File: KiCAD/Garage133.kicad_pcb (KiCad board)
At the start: 4 copper layers, 82.5 x 39.4 mm, 44 parts, among them J1 Edge2x6_Connector, J2 USB_B_Micro, K1 SANYOU_SRD_Form_C, K2 SANYOU_SRD_Form_C, Q2 UMH3N, Q3 MMBT3906, Q4 MMBT3906, U1 ESP32-WROOM-32, U2 AMS1117-3.3, U3 SHTC3

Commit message: Updated KiCAD design
Fixes with help from Gemini.

- 2 sonars per side
- Divide-down echo signal to be 3V input-safe
- Fix pin assignments to non-straping pins for relay control, to avoid opening the garage
   door on power on(!)
- 1mm traces for relay nets, to be safer in case someone wires more power through these
   connections.
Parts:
- removed the REF** at (70.4, 50.8)
- removed the REF** at (141.0, 50.8)
- removed the REF** at (141.0, 85.1)
- removed the REF** at (80.3, 52.1)
- added J_SNR3: Conn_01x04_Pin, Connector_JST:JST_XH_B4B-XH-A_1x04_P2.50mm_Vertical, F.Cu at (120.8, 52.1)
- added J_SNR4: Conn_01x04_Pin, Connector_JST:JST_XH_B4B-XH-A_1x04_P2.50mm_Vertical, F.Cu at (120.8, 61.0)
- added R2l1: 2.2k, Resistor_SMD:R_0603_1608Metric, F.Cu at (81.9, 55.9)
- added R2l2: 2.2k, Resistor_SMD:R_0603_1608Metric, F.Cu at (80.0, 55.9)
- added R2l3: 2.2k, Resistor_SMD:R_0603_1608Metric, F.Cu at (125.2, 57.1)
- added R2l4: 2.2k, Resistor_SMD:R_0603_1608Metric, F.Cu at (126.4, 66.7)
- added R3l1: 3.3k, Resistor_SMD:R_0603_1608Metric, F.Cu at (83.8, 55.9)
- added R3l2: 3.3k, Resistor_SMD:R_0603_1608Metric, F.Cu at (78.1, 55.9)
- added R3l3: 3.3k, Resistor_SMD:R_0603_1608Metric, F.Cu at (122.2, 57.1)
- added R3l4: 3.3k, Resistor_SMD:R_0603_1608Metric, F.Cu at (128.3, 66.7)
- added REF**: MountingHole_2.5mm, MountingHole:MountingHole_2.5mm, F.Cu at (156.2, 85.1)
- added REF**: MountingHole_2.5mm, MountingHole:MountingHole_2.5mm, F.Cu at (80.0, 51.4)
- added REF**: MountingHole_2.5mm, MountingHole:MountingHole_2.5mm, F.Cu at (156.2, 50.8)
- added REF**: MountingHole_2.5mm, MountingHole:MountingHole_2.5mm, F.Cu at (70.5, 50.8)
- added RTRL3: 1k, Resistor_SMD:R_0603_1608Metric, F.Cu at (69.2, 55.2)
- added RTRL4: 1k, Resistor_SMD:R_0603_1608Metric, F.Cu at (123.2, 66.7)
- J1: footprint Library:EdgeConnector_2x3 -> chl33_library:EdgeConnector_2x3
- moved K2 15.4 mm to (134.6, 76.3)
- moved K1 15.3 mm to (134.6, 59.1)
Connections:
- J_SNR1 pad 3: ECHO1 -> Net-(J_SNR1-Pin_3)
- J_SNR2 pad 3: ECHO2 -> Net-(J_SNR2-Pin_3)
- Q2 pad 2: RELAY_CMD1 -> unconnected-(Q2A-B1-Pad2)
- U1 pad 11: unconnected-(U1-IO26-Pad11) -> ECHO3
- U1 pad 12: unconnected-(U1-IO27-Pad12) -> TRIG4
- U1 pad 23: RELAY_CMD1 -> unconnected-(U1-IO15-Pad23)
- U1 pad 24: RELAY_CMD2 -> unconnected-(U1-IO2-Pad24)
- U1 pad 26: unconnected-(U1-IO4-Pad26) -> RELAY_CMD1
- U1 pad 31: unconnected-(U1-IO19-Pad31) -> RELAY_CMD2
- U1 pad 37: unconnected-(U1-IO23-Pad37) -> TRIG3
- U1 pad 8: unconnected-(U1-IO32-Pad8) -> ECHO4
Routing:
- net ECHO4: track 0.00 -> 73.3 mm, vias 0 -> 4
- net Net-(J_SNR3-Pin_2): track 0.00 -> 57.3 mm
- net ECHO3: track 0.00 -> 54.0 mm, vias 0 -> 3
- net TRIG4: track 0.00 -> 46.1 mm, vias 0 -> 3
- net Net-(J_SNR2-Pin_3): track 0.00 -> 24.0 mm, vias 0 -> 1
- net ECHO2: track 27.3 -> 4.98 mm, vias 1 -> 0
- net Net-(J_SNR1-Pin_3): track 0.00 -> 21.1 mm
- net ECHO1: track 23.5 -> 4.32 mm
- net RELAY2A: track 10.3 -> 27.1 mm
- net RELAY1B: track 24.7 -> 41.1 mm
- net Net-(D2-K): track 14.0 -> 29.6 mm
- net RELAY1A: track 9.87 -> 25.3 mm
- net RELAY2B: track 24.1 -> 39.1 mm
- net RELAY_CMD2: track 26.4 -> 37.7 mm, vias 3 -> 4
- net Net-(D1-K): track 23.8 -> 33.1 mm
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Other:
- board size 82.5 x 39.4 mm -> 97.8 x 39.4 mm
- board text added: "+5"
- board text added: "AL"
- board text added: "ECH"
- board text added: "EN"
- board text added: "GND"
- board text added: "GPIO"
- board text added: "Garage133 v2.0 (c) Chris Lee"
- board text added: "M1"
- board text added: "RX"
- board text added: "SCL"
- board text added: "SDA"
- board text added: "TRIG"
- board text added: "TX"
- board text added: "VBUS"
- board text removed: "Garage133 v1.3 (c) Chris Lee"

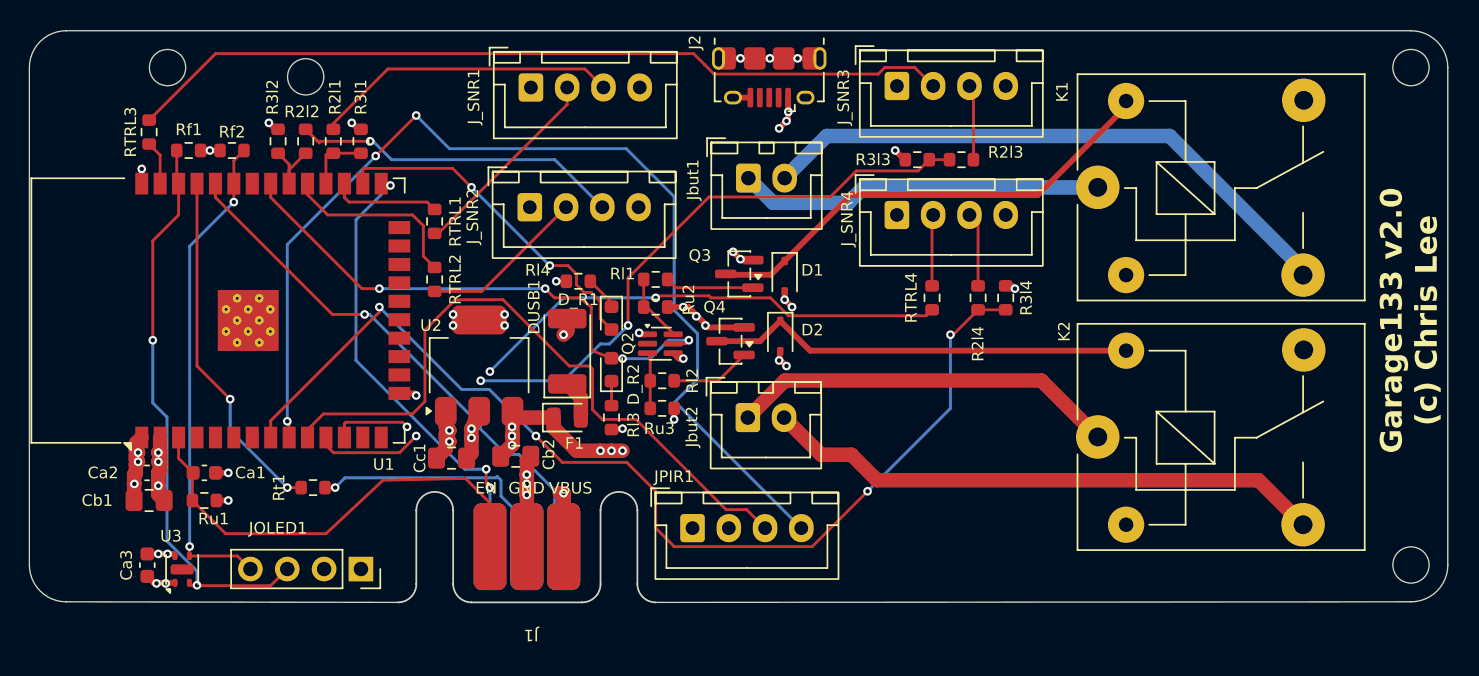
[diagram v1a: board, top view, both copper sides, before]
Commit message: KiCAD model: v2.1 fixes missing trace from Q2 pin2 to RELAY_CMD1
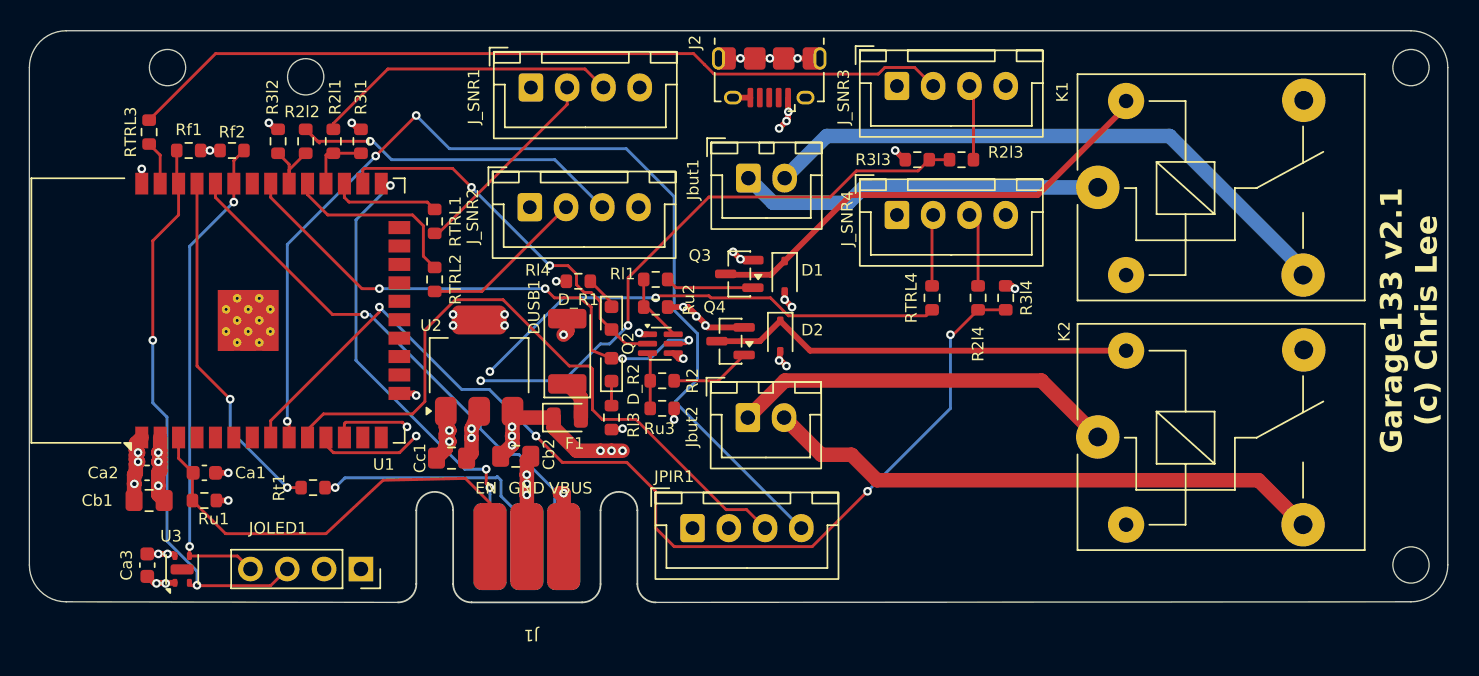
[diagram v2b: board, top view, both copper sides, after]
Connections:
- Q2 pad 2: unconnected-(Q2A-B1-Pad2) -> RELAY_CMD1
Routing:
- net RELAY_CMD1: track 23.8 -> 26.7 mm
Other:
- board text added: "Garage133 v2.1 (c) Chris Lee"
- board text removed: "Garage133 v2.0 (c) Chris Lee"
